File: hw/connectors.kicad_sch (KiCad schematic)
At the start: 4 parts, among them J1 Conn_02x04_Top_Bottom, J2 Analog, J8 SWD

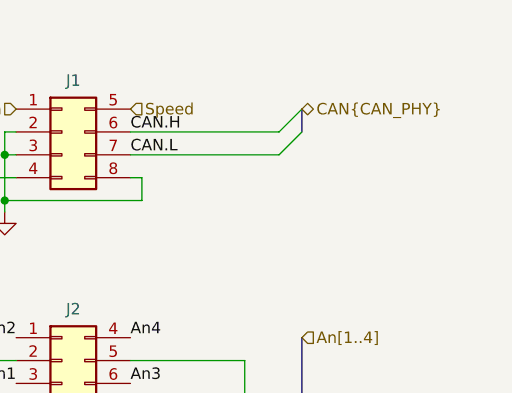
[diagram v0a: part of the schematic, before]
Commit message: hw: top level schematic
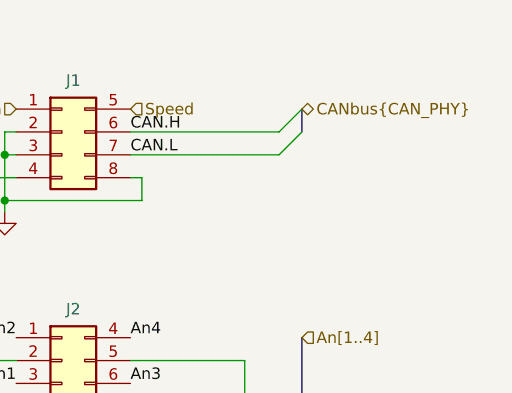
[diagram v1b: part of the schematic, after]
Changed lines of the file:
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@@
+		)
+	)
+	(hierarchical_label "CANbus{CAN_PHY}"
+		(shape bidirectional)
+		(at 76.2 38.1 0)
+		(effects
+			(font
+				(size 1.27 1.27)
+			)
+			(justify left)
 		)
 	)
@@
 		(effects
 			(font
-				(size 1.27 1.27)
-			)
-			(justify left)
-		)
-	)
-	(hierarchical_label "CAN{CAN_PHY}"
-		(shape bidirectional)
-		(at 76.2 38.1 0)
-		(effects
-			(font

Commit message: hw: erc: can
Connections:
- net CAN.H renamed CAN1.H
- net CAN.L renamed CAN1.L
